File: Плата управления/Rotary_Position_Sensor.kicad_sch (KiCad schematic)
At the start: 1 part, among them U6 AS5047D

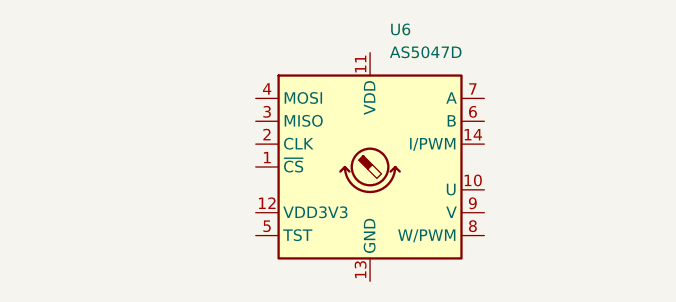
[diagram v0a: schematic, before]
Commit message: Заменил датчик положения ротора на NSM3012
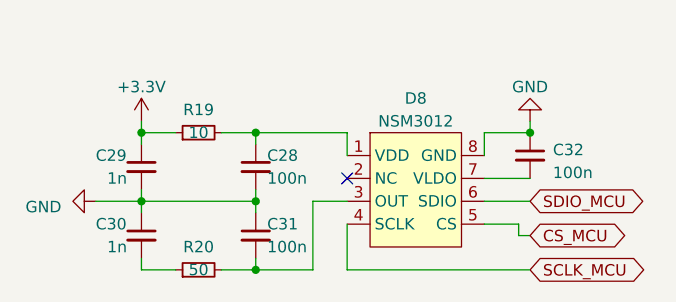
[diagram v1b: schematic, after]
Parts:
- removed U6: AS5047D, Package_SO:TSSOP-14_4.4x5mm_P0.65mm, symbol Sensor_Magnetic:AS5047D
- added C28, C31, C32: 100n, Capacitor_SMD:C_0603_1608Metric_Pad1.08x0.95mm_HandSolder, symbol Device:C_Small
- added C29, C30: 1n, Capacitor_SMD:C_0603_1608Metric_Pad1.08x0.95mm_HandSolder, symbol Device:C_Small
- added D8: NSM3012, symbol Hall_Sensor_My:NSM3012
- added R19: 10, Resistor_SMD:R_0603_1608Metric_Pad0.98x0.95mm_HandSolder, symbol Device:R_Small
- added R20: 50, Resistor_SMD:R_0603_1608Metric_Pad0.98x0.95mm_HandSolder, symbol Device:R_Small
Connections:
- new net: C28.1, D8.1 (VDD), R19.2
- new net: C31.2, D8.3 (OUT), R20.2
- new net: C32.2, D8.7 (VLDO)
- new net: C30.2, R20.1
- new net +3.3V: C29.1, R19.1
- new net CS_MCU: D8.5 (CS)
- new net GND: C28.2, C29.2, C30.1, C31.1, C32.1, D8.8 (GND)
- new net SCLK_MCU: D8.4 (SCLK)
- new net SDIO_MCU: D8.6 (SDIO)
- no-connect marks 0 -> 1

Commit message: Добавил 3.3В CAN SN65HVD232
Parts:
- D8: footprint (none) -> Package_SO:SOP-8_3.9x4.9mm_P1.27mm
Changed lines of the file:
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@@
       (effects (font (size 1.27 1.27)))
     )
-    (property "Footprint" "" (at 147.32 86.36 0)
+    (property "Footprint" "Package_SO:SOP-8_3.9x4.9mm_P1.27mm" (at 147.32 86.36 0)
       (effects (font (size 1.27 1.27)) hide)
     )

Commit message: Привел в порядок схему
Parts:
- renumbered C29 to C36, C30 to C37, C28 to C38, C31 to C39, C32 to C40, D8 to D7, R19 to R27, R20 to R28
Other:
- note added: "Датчик положения"
- moved on the sheet: C36, C37, C38, C39, C40, D7, R27, R28
